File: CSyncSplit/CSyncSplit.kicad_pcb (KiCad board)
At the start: 2 copper layers, 9 parts, among them CN1 JST_XH_B4B-XH-A_1x04_P2.50mm_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

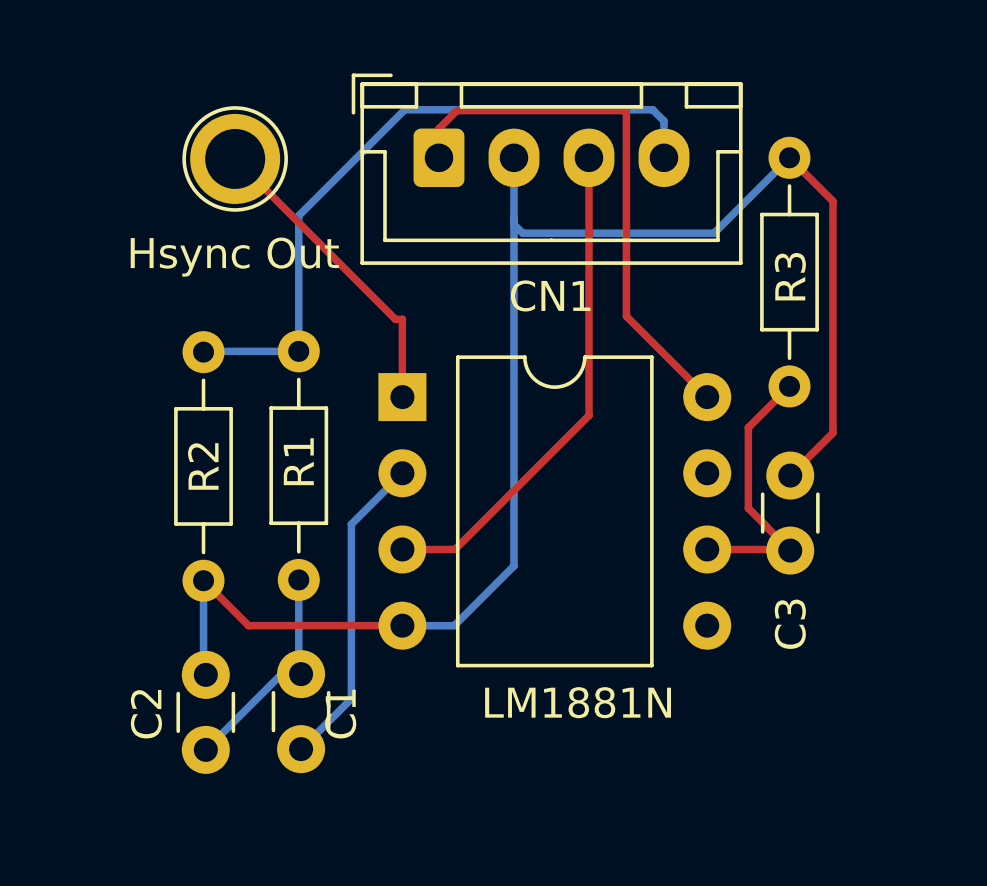
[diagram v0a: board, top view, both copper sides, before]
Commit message: CSyncSplitのパターンを修正 PCBのイメージを追加
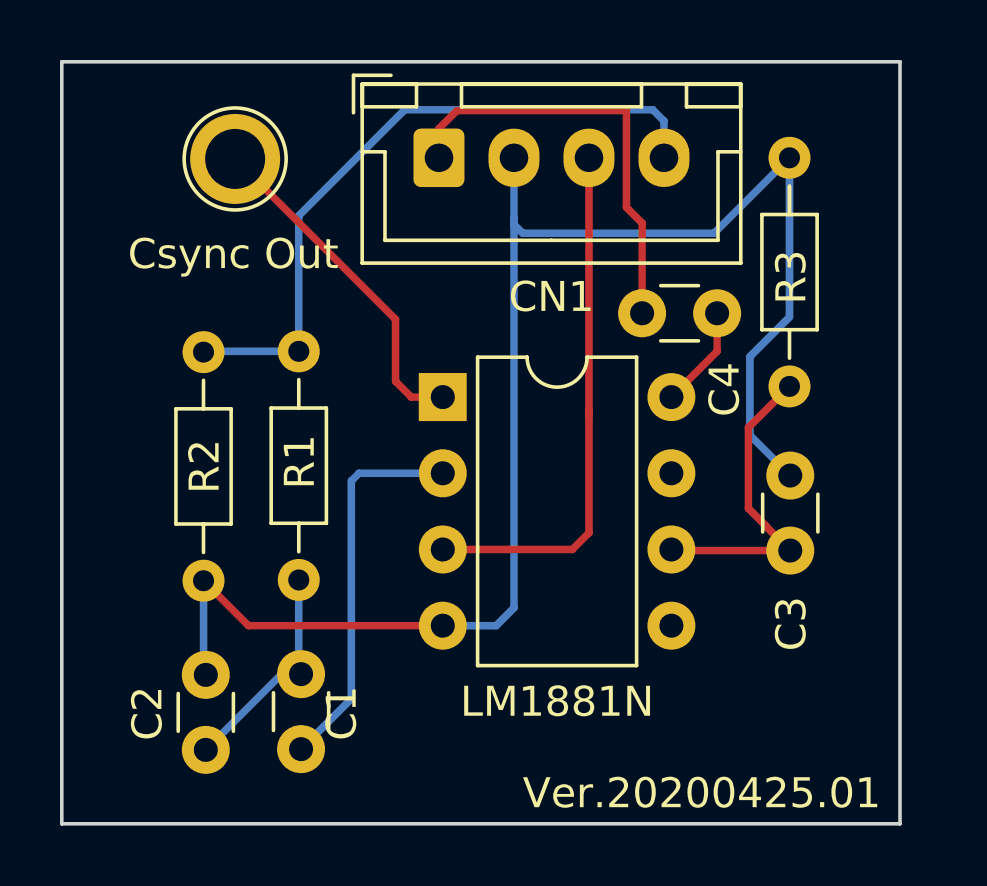
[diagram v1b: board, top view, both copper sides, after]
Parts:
- removed the LM1881N at (34.2, 26.4)
- added C4: C_Disc_D3.0mm_W1.6mm_P2.50mm, Capacitor_THT:C_Disc_D3.0mm_W1.6mm_P2.50mm, F.Cu at (44.7, 23.6)
- added LM1881N: DIP-8_W7.62mm, Package_DIP:DIP-8_W7.62mm, F.Cu at (35.6, 26.4)
- Csync Out: renamed from Hsync Out
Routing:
- net (no net): track 146.2 -> 152.4 mm
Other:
- board outline added: 27.9 x 25.4 mm
- board text added: "Ver.20200425.01"
